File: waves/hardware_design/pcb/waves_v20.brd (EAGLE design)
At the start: 82.2 x 107.2 mm, 110 parts, among them IC1 PCM5100PW, IC10 LD2981ABU33TR, IC2 STM32F405RGT6, IC3 1-2199298-2, IC4 1-2199298-2, IC5 MCP6004T-I_SL, IC7 TL072CD, IC8 LM4040C10IDBZR, IC9 LM1117DT-3.3_NOPB, J1 PJ301_THONKICONN6, J2 PJ301_THONKICONN6, J3 PJ301_THONKICONN6, J4 PJ301_THONKICONN6, J5 PJ301_THONKICONN6, J6 PJ301_THONKICONN6, J8 F31L-1A7H1-11030, Q1 CRYSTAL, U1 PEC11R-4215F-S0024

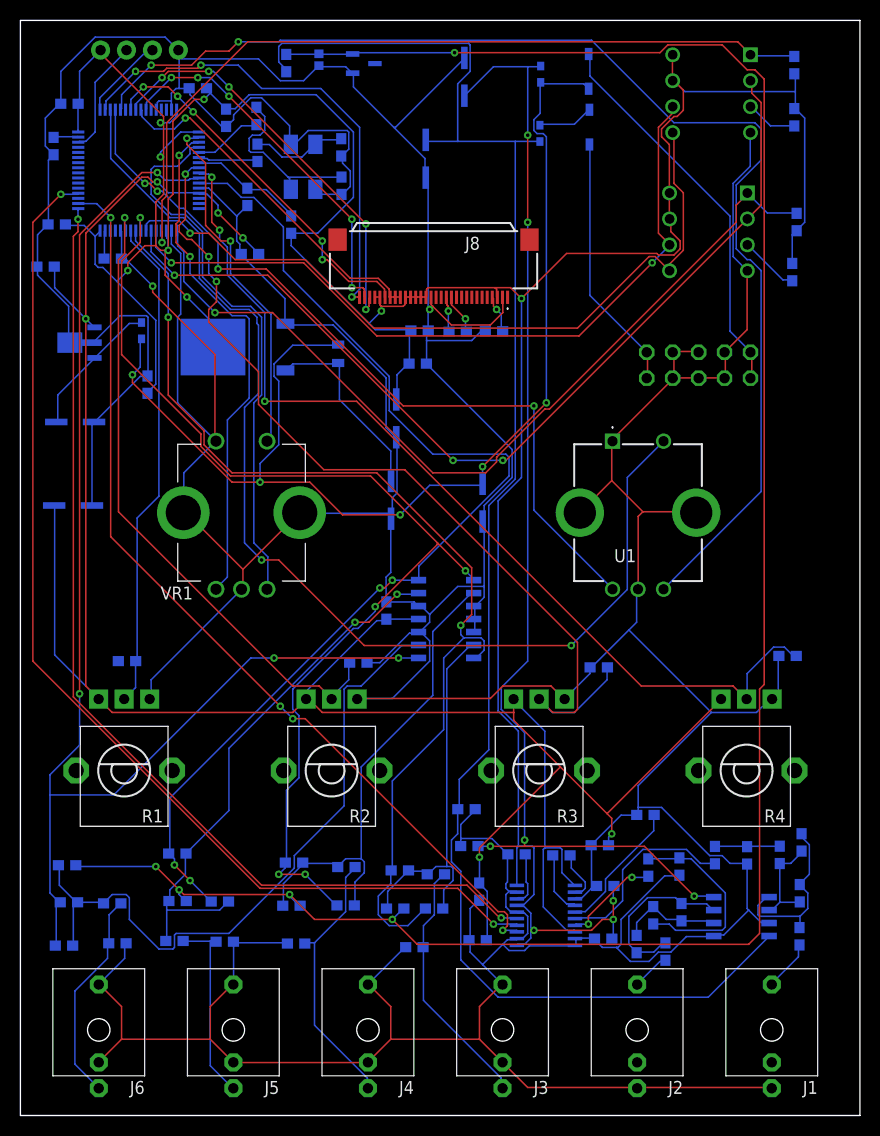
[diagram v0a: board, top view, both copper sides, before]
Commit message: schematic changes. handle +/- 10 volts. 0-8v for pitch
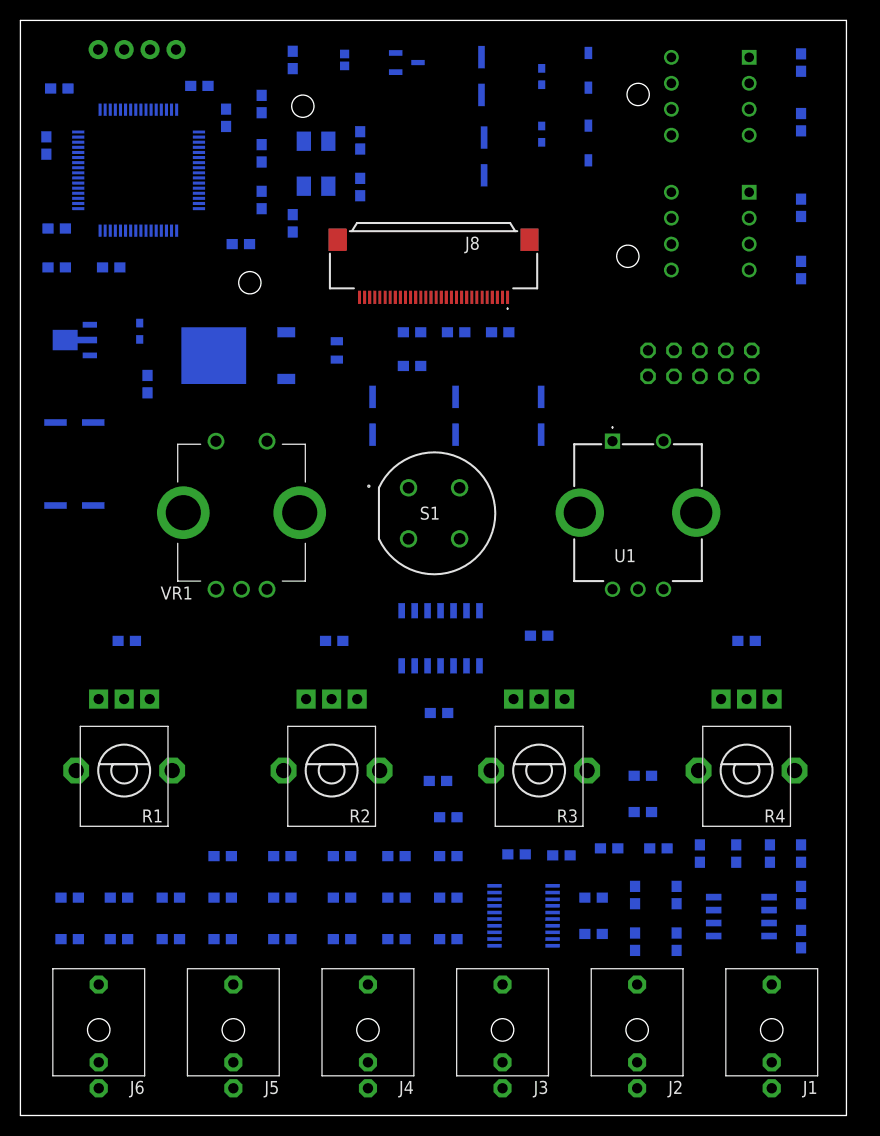
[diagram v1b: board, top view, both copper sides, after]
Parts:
- removed R30: 100k, SparkFun-Resistors:0603
- added S1: D6R90F1LFS, D6R Push Button:D6C10F1LFS
- R21: value 100k -> 80.6k
- R24, R27: value 100k -> 200k
- moved R22 37.3 mm to (41.9, 25.4)
- moved C43 11.3 mm to (41.0, 39.4), turned to 0 degrees
- moved C35 10.1 mm to (50.8, 68.6), turned to 270 degrees
- moved C37 8.62 mm to (34.3, 68.6), turned to 270 degrees
- moved C50 7.13 mm to (31.5, 17.3)
- moved C21 6.61 mm to (50.8, 47.0), turned to 180 degrees
- moved C41 6.42 mm to (61.0, 29.7), turned to 180 degrees
- moved C31 5.72 mm to (45.2, 94.0)
- moved C36 5.42 mm to (42.4, 68.6), turned to 270 degrees
- moved R32 4.75 mm to (36.8, 17.3)
- moved R26 4.45 mm to (19.8, 25.4)
- moved C20 4.28 mm to (71.1, 46.5), turned to 180 degrees
- moved IC8 4.22 mm to (37.8, 103.1)
- moved C28 3.93 mm to (40.9, 32.8)
- moved C6 3.84 mm to (61.0, 33.3)
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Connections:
- removed net N$28: C18.2
- new net BACK_BUTTON: IC2.38, S1.3, S1.4
- net AREF_-10: no longer R22.1
- net GND: now also C18.2, S1.1, S1.2
- net N$23: now also R22.1; no longer R30.1
- net VINA-: no longer R22.2
- net VIND-: now also R22.2; no longer R30.2
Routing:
- net GND: track 774.5 -> 0.00 mm, vias 2 -> 0
- net +3V3: track 334.6 -> 0.00 mm, vias 11 -> 0
- net +3V3_A: track 240.9 -> 0.00 mm, vias 6 -> 0
- net AREF_-10: track 207.7 -> 0.00 mm, vias 5 -> 0
- net VEE: track 160.4 -> 0.00 mm
- net ADC_TUNE_CV: track 127.7 -> 0.00 mm, vias 4 -> 0
- net ENC_1_B: track 121.2 -> 0.00 mm, vias 2 -> 0
- net N$22: track 113.3 -> 0.00 mm, vias 5 -> 0
- net VCC: track 112.2 -> 0.00 mm, vias 5 -> 0
- net ENC_1_CLICK: track 110.8 -> 0.00 mm, vias 2 -> 0
- net DAC_DIN: track 106.8 -> 0.00 mm, vias 2 -> 0
- net ADC_AMT_CV: track 106.8 -> 0.00 mm, vias 4 -> 0
- net ADC_FX_CV: track 106.5 -> 0.00 mm, vias 5 -> 0
- net ADC_MORPH_CV: track 103.1 -> 0.00 mm, vias 2 -> 0
- net DAC_LRCK: track 100.5 -> 0.00 mm, vias 2 -> 0
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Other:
- board size 82.2 x 107.2 mm -> 80.9 x 107.2 mm

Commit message: progress on audio DAC. switched to f446xx for now
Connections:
- net GND: now also J3.P1, J4.P1, J5.P1, J6.P1; no longer J3.P3, J4.P3, J5.P3, J6.P3
- net N$15: now also J5.P3; no longer J5.P1
- net N$16: now also J6.P3; no longer J6.P1
- net N$17: now also J4.P3; no longer J4.P1
- net N$23: now also J3.P3; no longer J3.P1

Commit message: starting to add xcode wavetable code
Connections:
- net N$3: now also J8.5; no longer J8.4
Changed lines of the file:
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@@
 <wire x1="11.299" y1="98.5072" x2="34.2122" y2="80.1292" width="0" layer="19" extent="1-16"/>
-</signal>
-<signal name="N$3">
-<contactref element="J8" pad="4"/>
-<contactref element="C17" pad="1"/>
-<wire x1="47.84" y1="76.708" x2="46.2122" y2="80.1292" width="0" layer="19" extent="1-16"/>
 </signal>
 <signal name="N$12">
@@
 <wire x1="5.6634" y1="91.3208" x2="43.013" y2="61.4768" width="0" layer="19" extent="16-16"/>
 </signal>
+<signal name="N$3">
+<contactref element="J8" pad="5"/>
+<contactref element="C17" pad="1"/>
+<wire x1="47.84" y1="76.708" x2="45.7122" y2="80.1292" width="0" layer="19" extent="1-16"/>
+</signal>
 </signals>
